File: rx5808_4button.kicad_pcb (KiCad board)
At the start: 2 copper layers, 53 parts, among them IC1 ATMEGA328-A, P1 CONN_01X02, P2 CONN_01X05, P3 CONN_02X03, P4 BNC, P5 BNC, P6 BNC, P7 CONN_01X02, SW1 SWITCH_INV, U1 TPS62160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

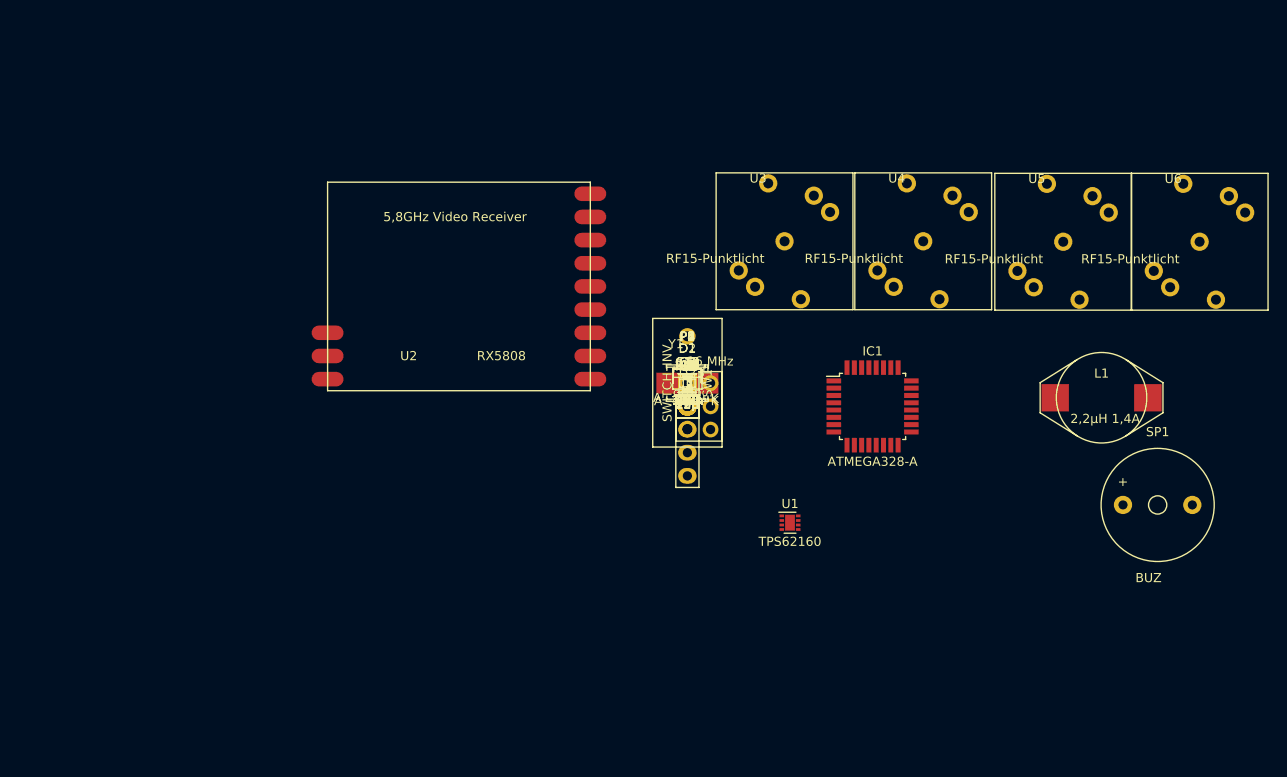
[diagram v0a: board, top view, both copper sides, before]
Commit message: Layout fertig und Footprint für SMA geaddet.
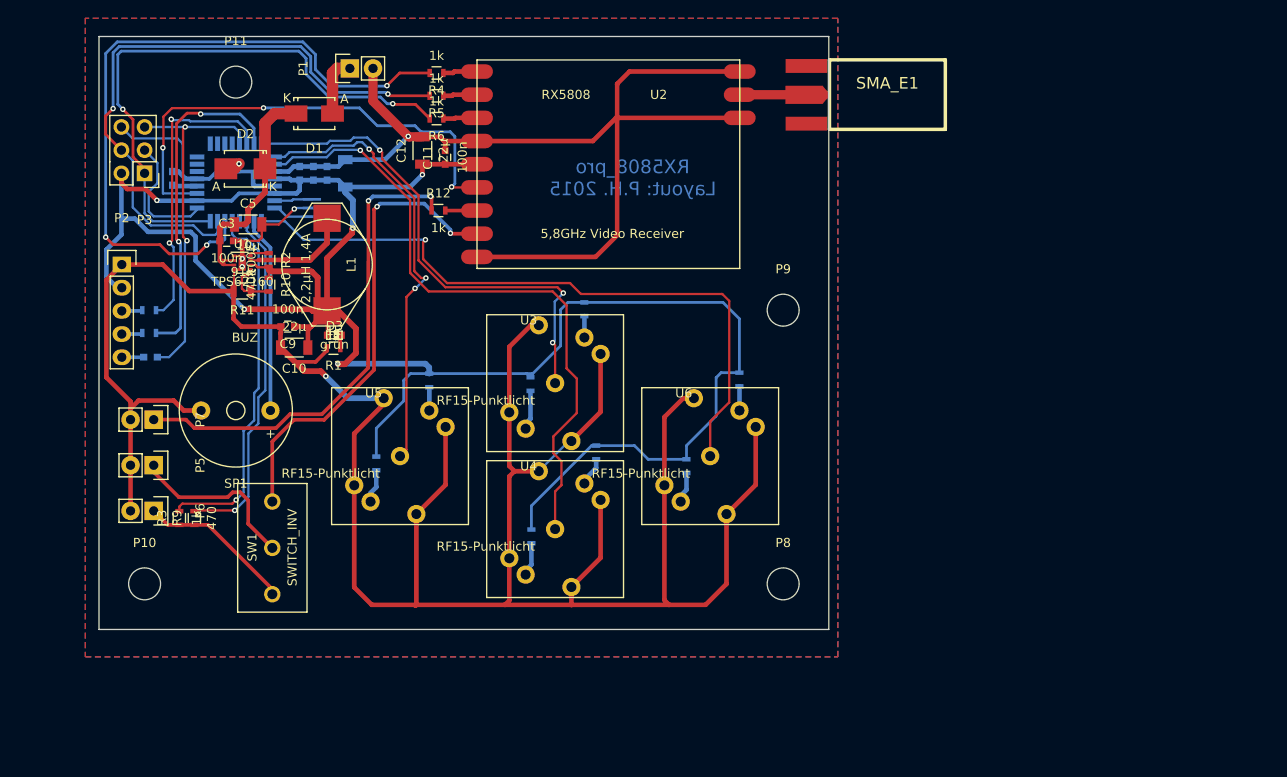
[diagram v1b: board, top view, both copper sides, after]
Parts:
- removed P4: BNC, Pin_Headers:Pin_Header_Straight_1x02
- added P10: CONN_01X01, Mounting_Holes:MountingHole_3-5mm, F.Cu at (89.0, 127.0)
- added P11: CONN_01X01, Mounting_Holes:MountingHole_3-5mm, F.Cu at (99.0, 72.0)
- added P8: CONN_01X01, Mounting_Holes:MountingHole_3-5mm, F.Cu at (159.0, 127.0)
- added P9: CONN_01X01, Mounting_Holes:MountingHole_3-5mm, F.Cu at (159.0, 97.0)
- added SMA_E1: SMA_EDGE, SMA_EDGE:SMA_EDGE, F.Cu at (170.4, 72.1)
- C1, C2, C4, C6, C7, C8, IC1, R13, R14, R15, R16, R17, R18, R19, R20, R7, R8, Y1: moved to B.Cu
- moved SP1 101.6 mm to (99.0, 108.0), turned to 180 degrees
- moved L1 86.1 mm to (109.0, 92.0), turned to 270 degrees
- moved U5 76.4 mm to (117.0, 113.0)
- moved IC1 74.0 mm to (99.0, 83.0), turned to 180 degrees
- moved U1 66.5 mm to (99.7, 91.8)
- moved P3 63.8 mm to (89.0, 82.0), turned to 180 degrees
- moved P2 63.4 mm to (86.5, 92.0)
- moved C1 60.8 mm to (92.0, 82.5), turned to 90 degrees
- moved P6 60.2 mm to (90.0, 119.0), turned to 270 degrees
- moved R7 59.5 mm to (89.5, 97.0)
- moved R8 59.3 mm to (89.5, 99.5)
- moved P5 59.2 mm to (90.0, 114.0), turned to 270 degrees
- moved C8 58.9 mm to (89.7, 102.2), turned to 180 degrees
- moved P7 58.6 mm to (90.0, 109.0), turned to 270 degrees
- moved U6 58.6 mm to (151.0, 113.0)
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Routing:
- net GND: track 0.00 -> 437.9 mm, vias 0 -> 6
- net +5V: track 0.00 -> 250.0 mm, vias 0 -> 5
- net Net-(IC1-Pad14): track 0.00 -> 76.2 mm, vias 0 -> 3
- net /save: track 0.00 -> 74.4 mm, vias 0 -> 1
- net /down: track 0.00 -> 71.1 mm, vias 0 -> 1
- net /mosi: track 0.00 -> 68.7 mm, vias 0 -> 2
- net /miso: track 0.00 -> 64.6 mm, vias 0 -> 2
- net /up: track 0.00 -> 55.5 mm, vias 0 -> 3
- net /rssi: track 0.00 -> 54.3 mm, vias 0 -> 3
- net Net-(P7-Pad1): track 0.00 -> 53.6 mm, vias 0 -> 2
- net Net-(SW1-Pad1): track 0.00 -> 51.7 mm, vias 0 -> 2
- net /mode: track 0.00 -> 49.1 mm, vias 0 -> 3
- net Net-(IC1-Pad13): track 0.00 -> 40.4 mm, vias 0 -> 1
- net /reset: track 0.00 -> 39.5 mm, vias 0 -> 2
- net Net-(IC1-Pad11): track 0.00 -> 38.4 mm, vias 0 -> 1
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- added copper zone on B.Cu, net GND
- added copper zone on F.Cu, net GND
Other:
- board outline added: 80 x 65 mm
- net class Default: clearance 0.254 -> 0.2032; trace_width 0.254 -> 0.3048; via_dia 0.889 -> 0.6; via_drill 0.635 -> 0.3
- rule trace_clearance: 0.254 -> 0.2032
- rule trace_min: 0.254 -> 0.1524
- rule via_min_drill: 0.508 -> 0.3
- rule via_min_size: 0.889 -> 0.5
- board text added: "RX5808_pro Layout: P.H. 2015"

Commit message: andere Spule und neues Layout für den Schaltwandler
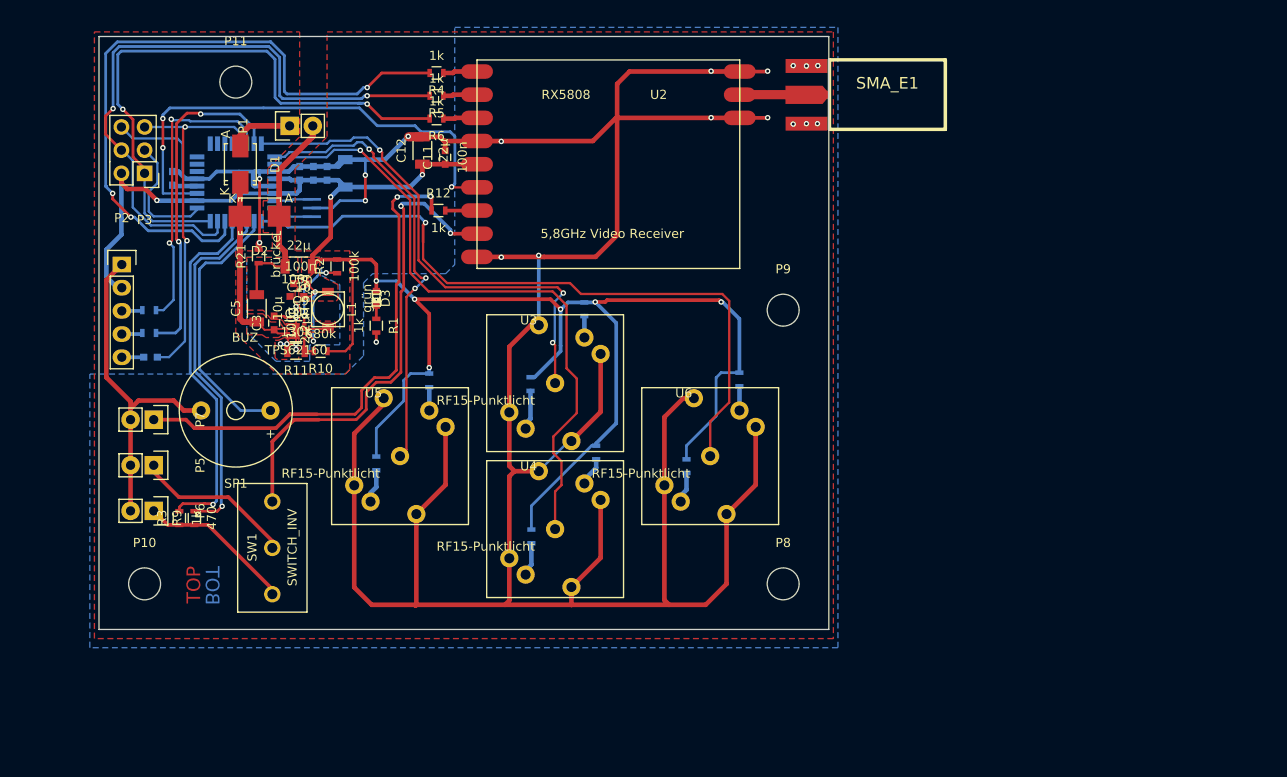
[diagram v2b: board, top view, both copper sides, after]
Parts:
- added C13: 100n, Capacitors_SMD:C_0603, F.Cu at (105.7, 95.5)
- added R21: brücke, Resistors_SMD:R_0603, F.Cu at (101.5, 91.1)
- L1: value 2,2µH 1,4A -> 2,2µH 5,9A; footprint Inductors:self_cms_we-pd3 -> TDK_Inductor:VLF4012A
- R10: value 470k -> 680k
- R11: value 91k -> 130k
- moved C3 10.4 mm to (103.2, 98.4), turned to 90 degrees
- moved D1 9.82 mm to (99.5, 81.0), turned to 270 degrees
- moved U1 9.54 mm to (105.6, 99.3)
- moved R10 9.26 mm to (108.3, 101.5), turned to 180 degrees
- moved C5 9.25 mm to (101.3, 96.8), turned to 90 degrees
- moved P1 9.12 mm to (104.9, 76.8)
- moved C10 8.91 mm to (105.9, 92.2)
- moved R11 8.85 mm to (105.6, 101.5)
- moved R2 7.53 mm to (110.1, 92.2), turned to 90 degrees
- moved D3 6.12 mm to (114.4, 95.7), turned to 270 degrees
- moved D2 5.43 mm to (101.6, 86.7), turned to 180 degrees
- moved R1 5.31 mm to (114.4, 98.7), turned to 270 degrees
- moved C9 4.90 mm to (106.1, 94.1)
- moved L1 4.90 mm to (109.1, 96.9), turned to 90 degrees
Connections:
- C10 pad 2: GND -> GNDPWR
- C3 pad 2: GND -> GNDPWR
- C5 pad 2: GND -> GNDPWR
- C9 pad 2: GND -> GNDPWR
- D2 pad 1: GND -> GNDPWR
- IC1 pad 12: (no net) -> Net-(IC1-Pad12)
- IC1 pad 22: (no net) -> Net-(IC1-Pad22)
- IC1 pad 23: (no net) -> Net-(IC1-Pad23)
- IC1 pad 24: (no net) -> Net-(IC1-Pad24)
- IC1 pad 25: (no net) -> Net-(IC1-Pad25)
- IC1 pad 26: (no net) -> Net-(IC1-Pad26)
- IC1 pad 27: (no net) -> Net-(IC1-Pad27)
- IC1 pad 28: (no net) -> Net-(IC1-Pad28)
- P1 pad 2: GND -> GNDPWR
- P10 pad 1: (no net) -> Net-(P10-Pad1)
- P11 pad 1: (no net) -> Net-(P11-Pad1)
- P8 pad 1: (no net) -> Net-(P8-Pad1)
- P9 pad 1: (no net) -> Net-(P9-Pad1)
- R11 pad 2: GND -> GNDPWR
- U1 pad 1: GND -> GNDPWR
- U1 pad 4: GND -> GNDPWR
- U1 pad EP: GND -> GNDPWR
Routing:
- net GNDPWR: track 0.00 -> 36.3 mm, vias 0 -> 7
- net GND: track 437.9 -> 421.1 mm, vias 6 -> 19
- net Net-(L1-Pad1): track 12.2 -> 2.70 mm
- net /buzzer: track 21.5 -> 29.4 mm
- net +5V: track 250.0 -> 242.9 mm, vias 5 -> 11
- net Net-(R2-Pad1): track 2.21 -> 8.32 mm, vias 0 -> 2
- net +12V: track 26.0 -> 22.4 mm
- net Net-(R10-Pad2): track 5.95 -> 2.47 mm
- net Net-(IC1-Pad14): track 76.2 -> 74.0 mm
- net Net-(P7-Pad1): track 53.6 -> 55.7 mm
- net /save: track 74.4 -> 76.5 mm
- net Net-(SW1-Pad1): track 51.7 -> 53.6 mm
- net /miso: track 64.6 -> 66.4 mm
- net /mosi: track 68.7 -> 70.4 mm
- net Net-(P5-Pad1): track 19.1 -> 17.6 mm
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- added copper zone on F.Cu, net +12V
- added copper zone on F.Cu, net +5V
- added copper zone on B.Cu, net GNDPWR
- added copper zone on F.Cu, net GNDPWR
- added copper zone on F.Cu, net Net-(L1-Pad1)
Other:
- board text added: "BOT"
- board text added: "TOP"
- board text removed: "RX5808_pro Layout: P.H. 2015"

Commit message: Schaltwandler weiter verbessert
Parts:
- moved C9 2.33 mm to (105.7, 96.4)
- moved C10 1.10 mm to (105.9, 93.3)
- moved R10 0.72 mm to (107.9, 102.1), turned to 270 degrees
- moved C13 0.40 mm to (105.7, 95.1)
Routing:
- net +5V: track 242.9 -> 229.9 mm
- net Net-(R10-Pad2): track 2.47 -> 3.94 mm
- net GNDPWR: track 36.3 -> 35.0 mm, vias 7 -> 8

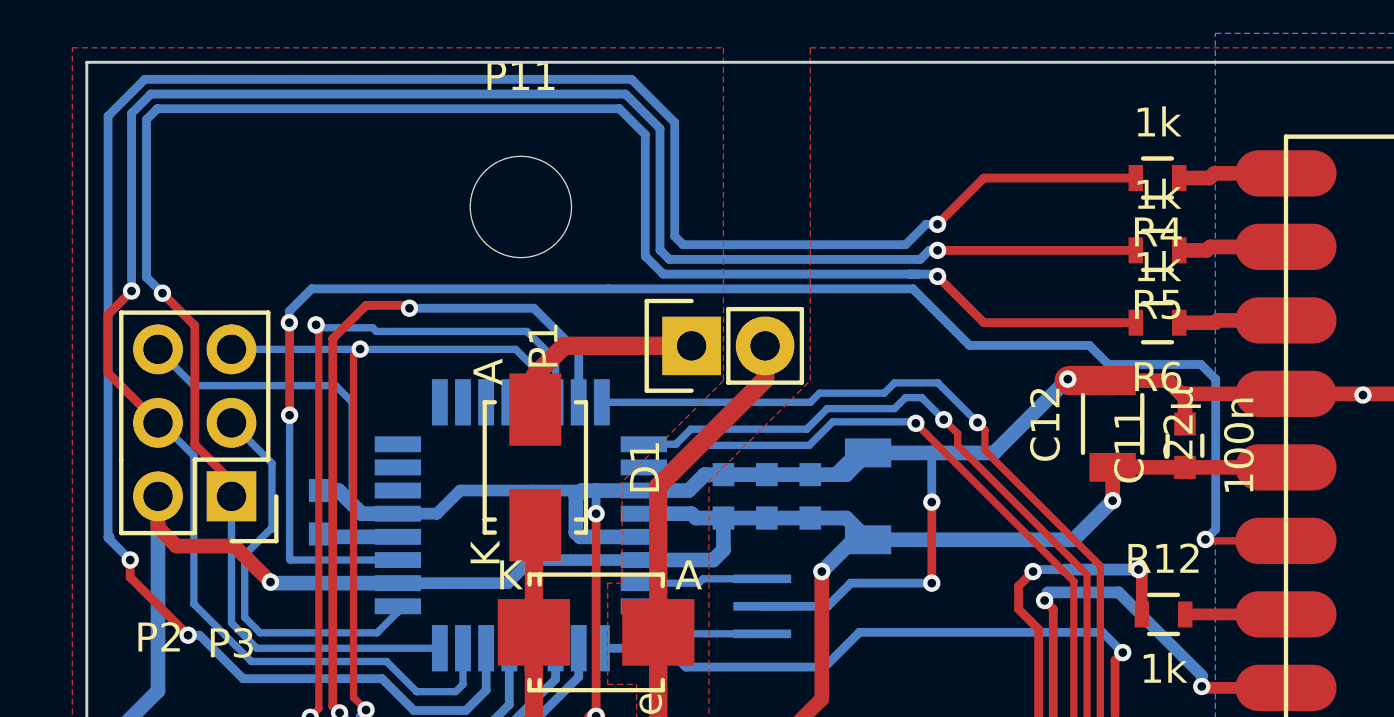
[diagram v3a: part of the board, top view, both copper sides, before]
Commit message: finale änderungen an Leiterbahnen
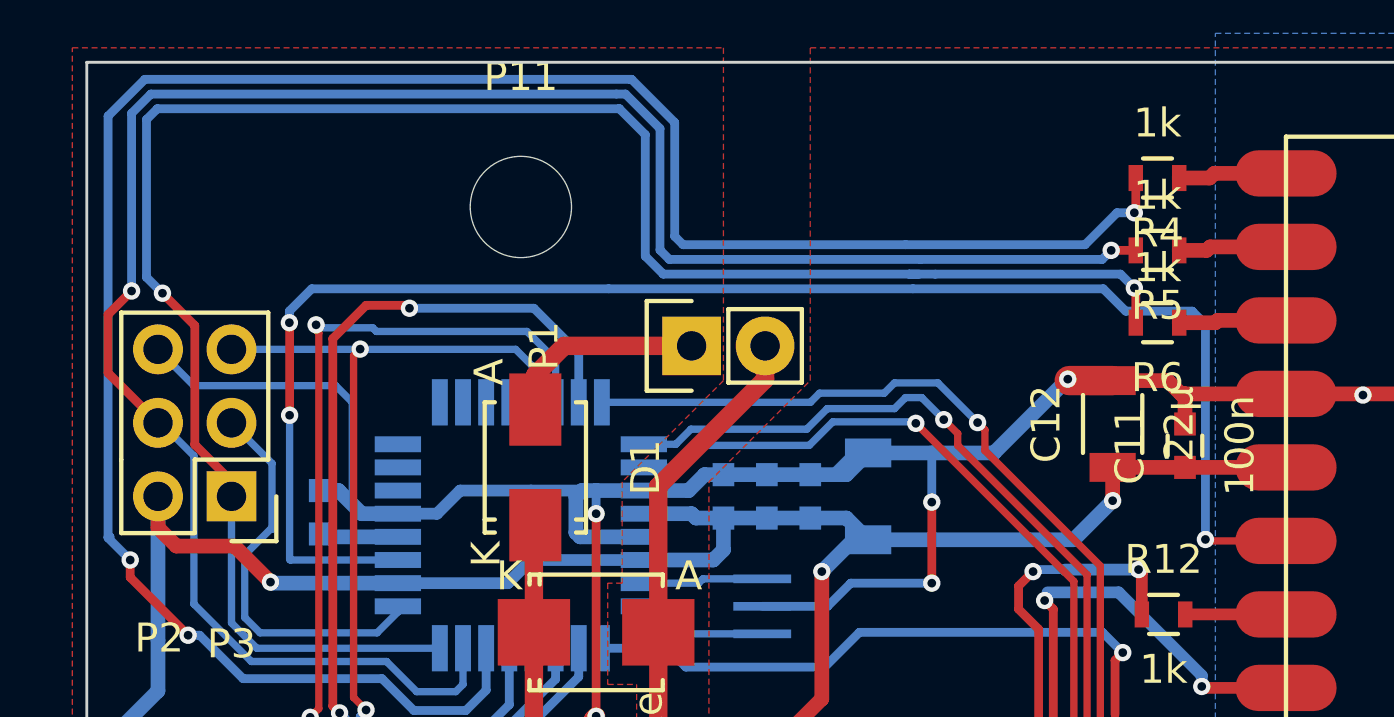
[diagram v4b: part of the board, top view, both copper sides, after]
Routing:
- net /miso: track 66.4 -> 67.1 mm
- net Net-(IC1-Pad14): track 74.0 -> 74.7 mm
- net /rssi: track 54.5 -> 55.1 mm
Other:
- rule pad_to_mask_clearance: 0 -> 0.1

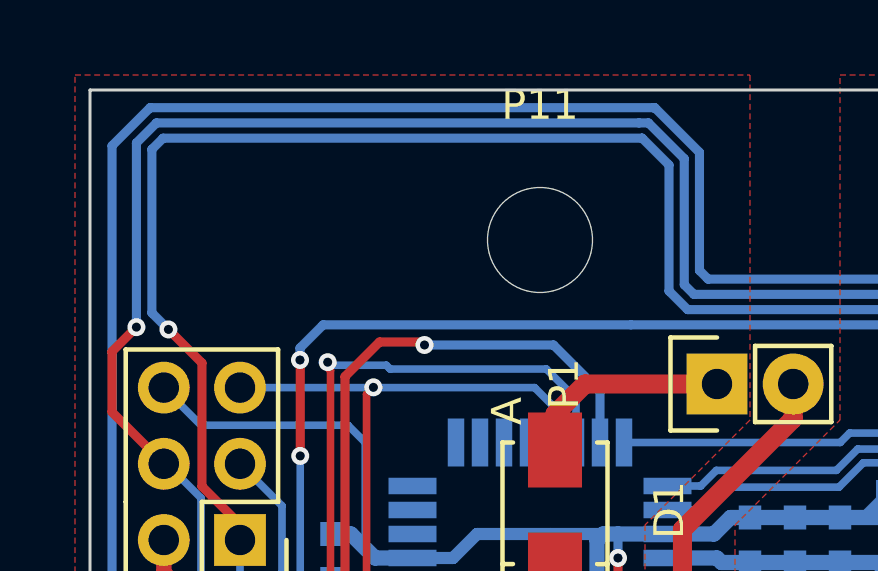
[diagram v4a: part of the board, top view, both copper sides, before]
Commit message: rssi-anschluss für externe RSSI-Anzeige dazugebaut
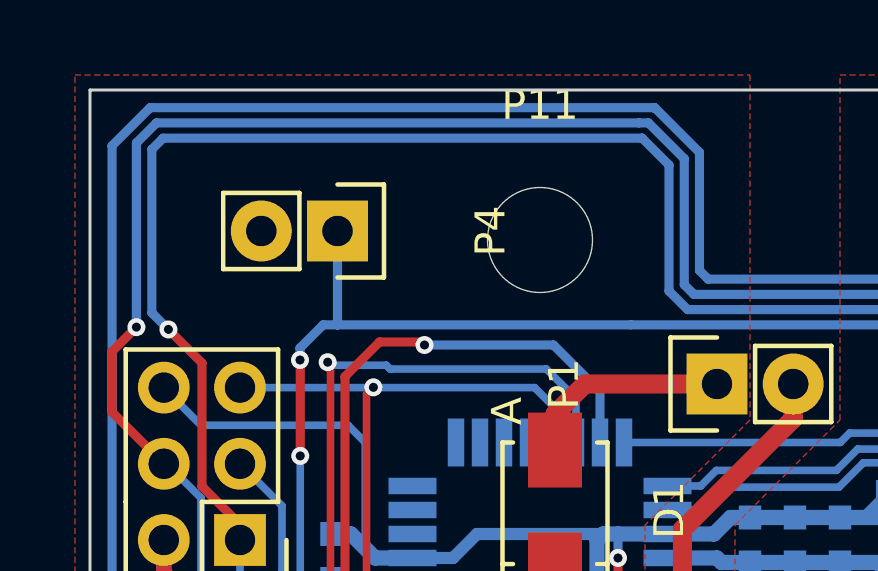
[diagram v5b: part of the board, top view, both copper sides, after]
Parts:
- added P4: CONN_01X02, Pin_Headers:Pin_Header_Straight_1x02, F.Cu at (92.2, 71.7)
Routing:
- net /rssi: track 55.1 -> 58.3 mm
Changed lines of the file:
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@@
 (kicad_pcb (version 4) (host pcbnew "(2014-08-05 BZR 5054)-product")
   (general
-    (links 134)
+    (links 136)
     (no_connects 0)
-    (area 81.388467 60.150001 182 140.700001)
+    (area 83.949999 66.949999 164.050001 132.050001)
     (thickness 1.6)
     (drawings 12)
-    (tracks 741)
+    (tracks 745)
     (zones 0)
-    (modules 59)
+    (modules 60)
     (nets 60)
   )
@@
     (visible_elements FFFFFF1F)
     (pcbplotparams
-      (layerselection 0x00030_80000001)
-      (usegerberextensions false)
+      (layerselection 0x010c0_80000001)
+      (usegerberextensions true)
       (excludeedgelayer true)
       (linewidth 0.100000)
@@
       (outputformat 1)
       (mirror false)
-      (drillshape 1)
+      (drillshape 0)
       (scaleselection 1)
-      (outputdirectory ""))
+      (outputdirectory gerber/))
   )
   (net 0 "")
@@
     (pad 2 smd rect (at 1.9 0 90) (size 0.9 1.3) (layers F.Cu F.Mask)
       (net 3 +5V))
+  )
+  (module Pin_Headers:Pin_Header_Straight_1x02 (layer F.Cu)
+    (at 92.25 71.7 270)
+    (descr "Through hole pin header")
+    (tags "pin header")
+    (fp_text reference P4 (at 0 -5.1 270) (layer F.SilkS)
+      (effects (font (size 1 1) (thickness 0.15)))
+    )
+    (fp_text value CONN_01X02 (at 0 -3.1 270) (layer F.SilkS) hide
+      (effects (font (size 1 1) (thickness 0.15)))
+    )
+    (fp_line (start 1.27 1.27) (end 1.27 3.81) (layer F.SilkS) (width 0.15))
+    (fp_line (start 1.55 -1.55) (end 1.55 0) (layer F.SilkS) (width 0.15))
+    (fp_line (start -1.75 -1.75) (end -1.75 4.3) (layer F.CrtYd) (width 0.05))
+    (fp_line (start 1.75 -1.75) (end 1.75 4.3) (layer F.CrtYd) (width 0.05))
+    (fp_line (start -1.75 -1.75) (end 1.75 -1.75) (layer F.CrtYd) (width 0.05))
+    (fp_line (start -1.75 4.3) (end 1.75 4.3) (layer F.CrtYd) (width 0.05))
+    (fp_line (start 1.27 1.27) (end -1.27 1.27) (layer F.SilkS) (width 0.15))
+    (fp_line (start -1.55 0) (end -1.55 -1.55) (layer F.SilkS) (width 0.15))
+    (fp_line (start -1.55 -1.55) (end 1.55 -1.55) (layer F.SilkS) (width 0.15))
+    (fp_line (start -1.27 1.27) (end -1.27 3.81) (layer F.SilkS) (width 0.15))
+    (fp_line (start -1.27 3.81) (end 1.27 3.81) (layer F.SilkS) (width 0.15))
+    (pad 1 thru_hole rect (at 0 0 270) (size 2.032 2.032) (drill 1.016) (layers *.Cu *.Mask F.SilkS)
+      (net 21 /rssi))
+    (pad 2 thru_hole oval (at 0 2.54 270) (size 2.032 2.032) (drill 1.016) (layers *.Cu *.Mask F.SilkS)
+      (net 2 GND))
+    (model Pin_Headers/Pin_Header_Straight_1x02.wrl
+      (at (xyz 0 -0.05000000074505806 0))
+      (scale (xyz 1 1 1))
+      (rotate (xyz 0 0 90))
+    )
   )
   (gr_text BOT (at 96.4 127.2 270) (layer B.Cu)
@@
   (segment (start 94.75 85.9964) (end 94.0308 86.7156) (width 0.254) (layer B.Cu) (net 20) (status 10))
   (segment (start 94.75 85.8) (end 94.75 85.9964) (width 0.254) (layer B.Cu) (net 20) (status 30))
+  (segment (start 92.25 71.7) (end 92.25 74.8284) (width 0.3048) (layer B.Cu) (net 21))
+  (segment (start 92.25 74.8284) (end 92.25 74.8) (width 0.3048) (layer B.Cu) (net 21))
+  (segment (start 92.25 74.8) (end 92.25 74.8284) (width 0.3048) (layer B.Cu) (net 21))
   (segment (start 112.5474 74.8284) (end 119.1284 74.8284) (width 0.3048) (layer B.Cu) (net 21))
   (segment (start 91 76) (end 91 75.6) (width 0.3048) (layer B.Cu) (net 21))
@@
   (segment (start 91.0082 79.1972) (end 91.0082 76.0082) (width 0.3048) (layer F.Cu) (net 21))
   (segment (start 102.0318 74.8284) (end 112.5474 74.8284) (width 0.3048) (layer B.Cu) (net 21))
-  (segment (start 102.0318 74.8284) (end 91.7716 74.8284) (width 0.3048) (layer B.Cu) (net 21))
+  (segment (start 102.0318 74.8284) (end 92.25 74.8284) (width 0.3048) (layer B.Cu) (net 21))
+  (segment (start 92.25 74.8284) (end 91.7716 74.8284) (width 0.3048) (layer B.Cu) (net 21))
   (segment (start 91 75.6) (end 91.7716 74.8284) (width 0.3048) (layer B.Cu) (net 21))
   (segment (start 122.6566 76.0566) (end 122.6566 83.4898) (width 0.3048) (layer B.Cu) (net 21))
